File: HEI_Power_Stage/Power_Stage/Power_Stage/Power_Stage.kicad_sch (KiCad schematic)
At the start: 44 parts, among them J2 Conn_02x10_Odd_Even, J3 Screw_Terminal_01x01, J4 Screw_Terminal_01x01, J5 OSTTA020161, J5 Screw_Terminal_01x01, U1 TBA 2-1212, U13 TPS73250DBVR, U14 TPS73250DBVR, U15 ADC124S051CIMM/NOPB, U17 TPS73250DBVR, U2 1769205241, U3 TPS73250DBVR

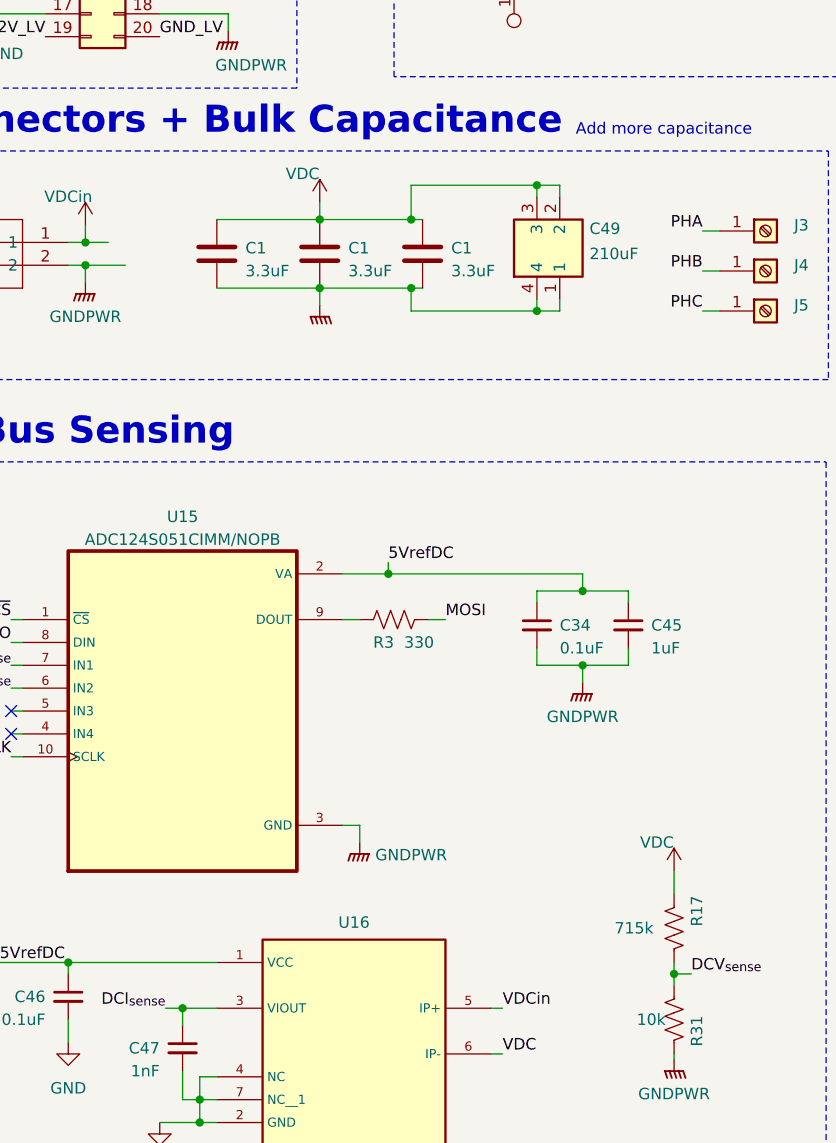
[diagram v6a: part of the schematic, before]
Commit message: POC layout changes fro meeting
Two cap options on the bottom:
large kemet that would meet all requirements on its own
also large cylindrical aluminum electrolytic that only has 4.3A riplpe current rating. can use either for testing. can also add more holes for trying other caps

layer 3 now continous gndpwr for whole board.
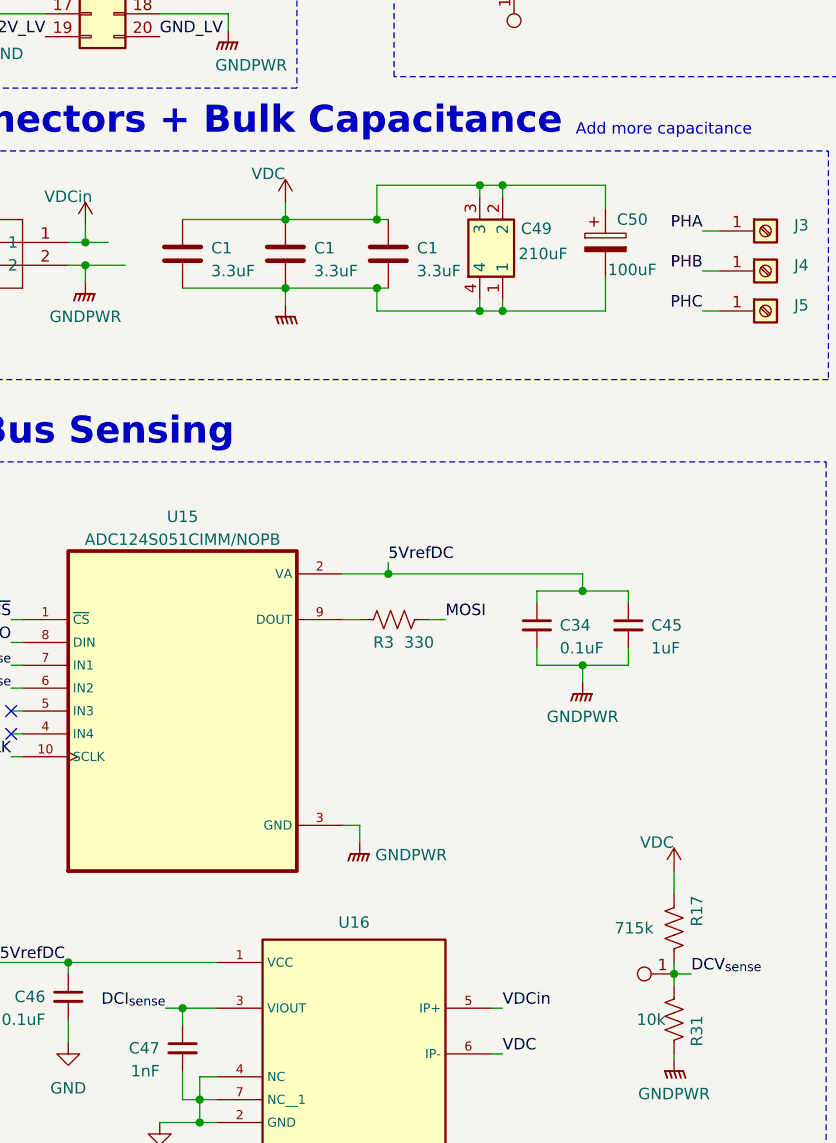
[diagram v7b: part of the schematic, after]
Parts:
- added C50: 100uF, Capacitor_THT:CP_Radial_D35.0mm_P10.00mm_SnapIn, symbol Device:C_Polarized
- added TP17: Test_Point, TestPoint:TestPoint_Pad_D1.0mm, symbol GTSR_symbol_lib:Test_Point
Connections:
- net DCV_{sense}: now also TP17.1
- net GNDPWR: now also C50.2
- net VDC: now also C50.1
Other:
- moved on the sheet: C1, C49

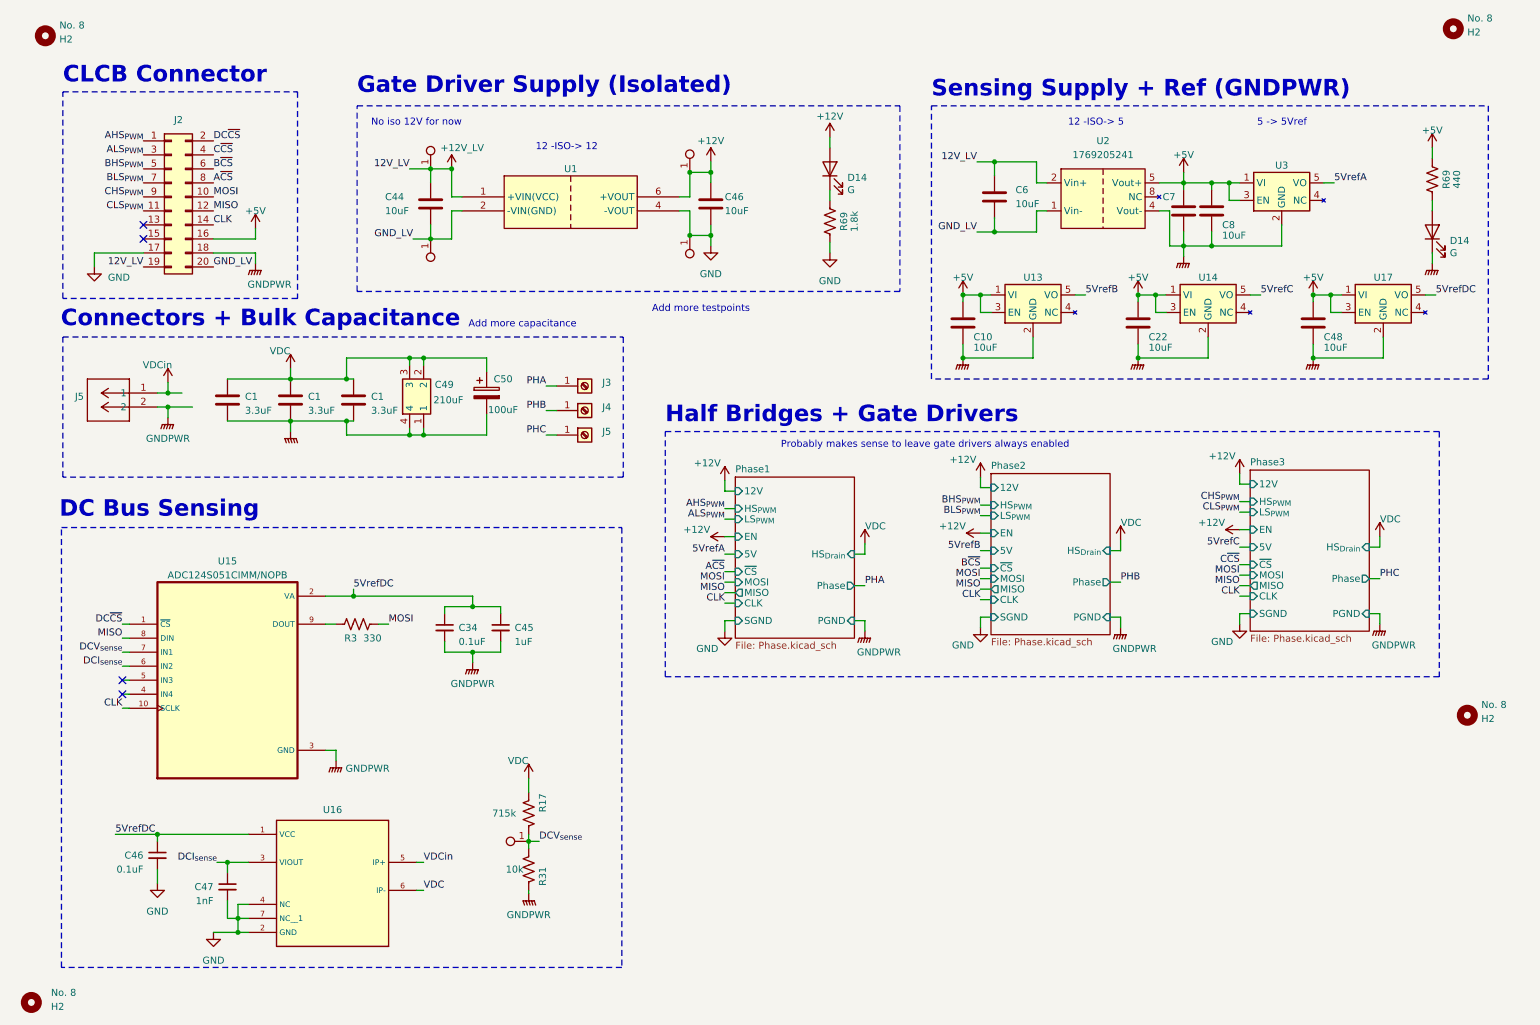
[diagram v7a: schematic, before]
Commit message: added low pass filters, PGND/SGND jumper
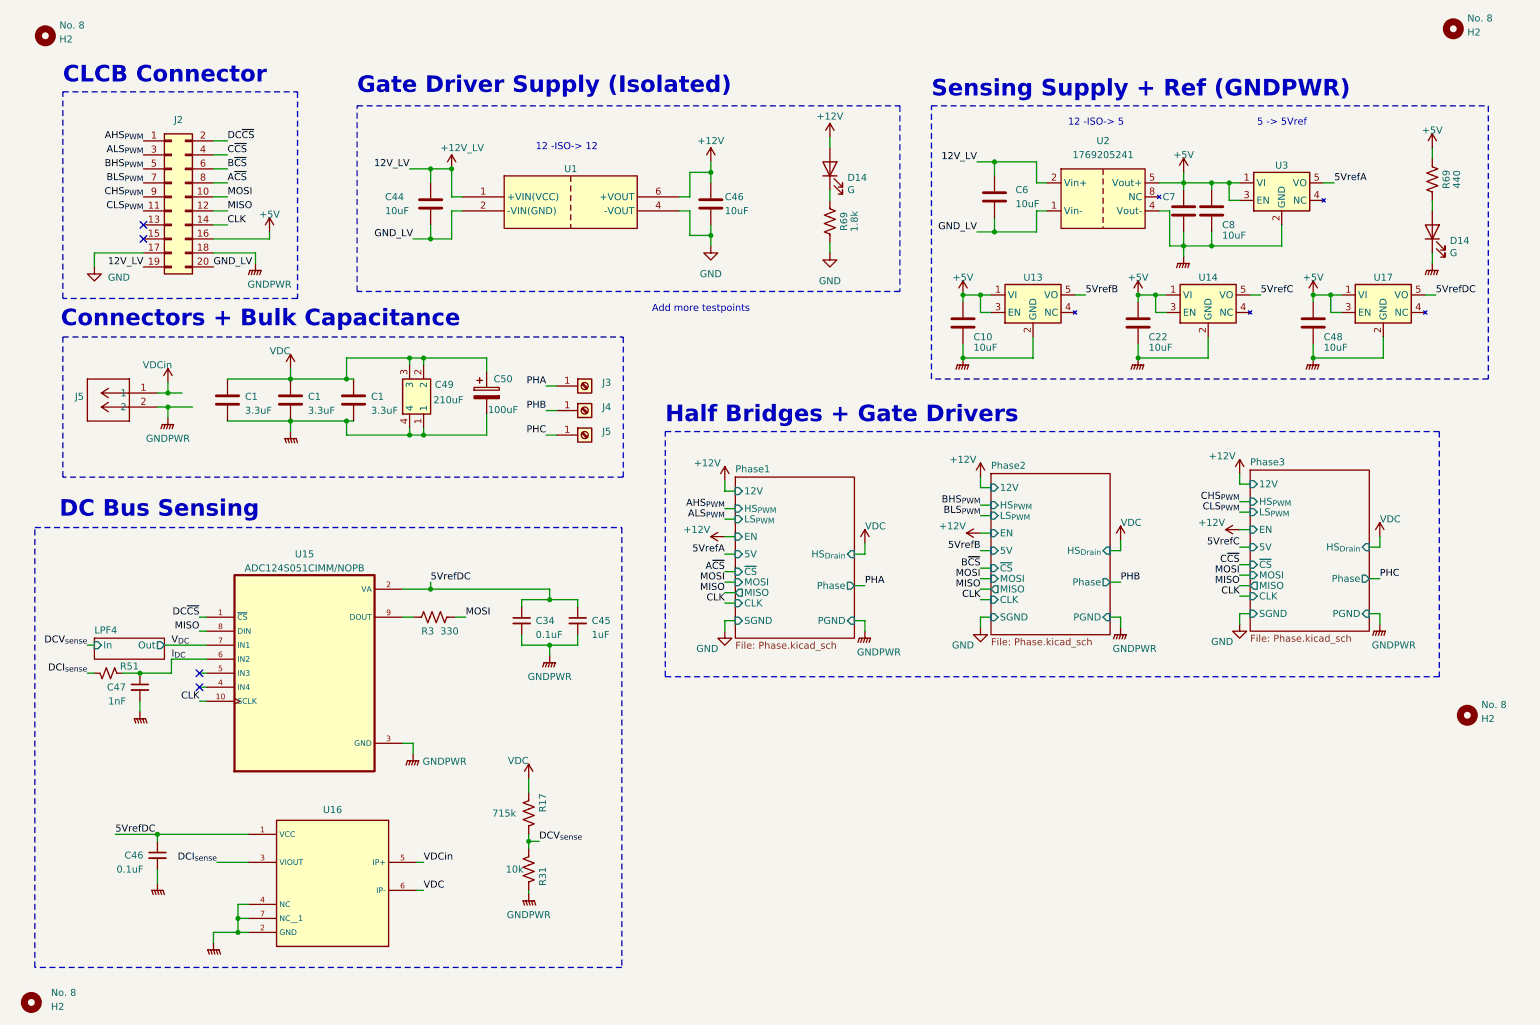
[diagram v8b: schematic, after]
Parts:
- removed TP1, TP17, TP2, TP3, TP4: Test_Point, TestPoint:TestPoint_Pad_D1.0mm, symbol GTSR_symbol_lib:Test_Point
- added R51: 2.2 0.1W, Resistor_SMD:R_0402_1005Metric_Pad0.72x0.64mm_HandSolder, symbol Device:R_Small_US
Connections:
- net DCI_{sense}: now also R51.2; no longer C47.1, U15.6 (IN2)
- net DCV_{sense}: no longer U15.7 (IN1)
- net GND: no longer C46.2, C47.2, U16.2 (GND), U16.4 (NC), U16.7 (NC__1)
- net GNDPWR: now also C46.2, C47.2, U16.2 (GND), U16.4 (NC), U16.7 (NC__1)
- new net I_{DC}: C47.1, R51.1, U15.6 (IN2)
- new net V_{DC}: U15.7 (IN1)
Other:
- added sheet LPF4 (LPF.kicad_sch)
- note removed: "Add more capacitance"
- note removed: "No iso 12V for now"
- note removed: "Probably makes sense to leave gate drivers always enabled"
- moved on the sheet: C34, C45, R3, U15
